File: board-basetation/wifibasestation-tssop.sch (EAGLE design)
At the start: 22 parts, among them IC1 1117EMP, J1 SWD_SHROUD_SMD, X1 ESP-03, X2 SMA-142-0711-821/826

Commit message: something changed
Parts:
- removed R1: 10k, passives-7351:RESISTOR0603-N
- removed R6: 4k7, passives-7351:RESISTOR0603-N
- added JP1: FTDI_BASICPTH, SparkFun-Connectors:FTDI_BASICPTH
- added RN2: 10k, resistor-dil:4R-NEXB38V
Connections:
- removed net N$18: R1.P$2, S1.1, U$1.BOOT0
- new net N$2: RN2B.1, S1.1, U$1.BOOT0
- new net N$8: RN2D.1, X1.GPIO2
- net +3V3: now also RN2D.2; no longer R6.P$1
- net GND: now also RN2A.2, RN2B.2, RN2C.2; no longer R1.P$1
- net GPIO0: now also RN2A.1
- net GPIO15: now also RN2C.1
- net N$1: no longer R6.P$2, X1.GPIO2
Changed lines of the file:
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@@
 <part name="C6" library="passives-7351" deviceset="CAPACITOR" device="0603-N" value="100n"/>
 <part name="C4" library="passives-7351" deviceset="CAPACITOR" device="0603-N" value="100n"/>
-<part name="R1" library="passives-7351" deviceset="RESISTOR" device="0603-N" value="10k"/>
 <part name="GND7" library="supply1" deviceset="GND" device=""/>
 <part name="J1" library="dtb" deviceset="SWD_SHROUD" device="_SMD" value="SWD_SHROUD_SMD"/>
@@
 <part name="GND22" library="supply1" deviceset="GND" device=""/>
 <part name="+3V14" library="supply1" deviceset="+3V3" device=""/>
-<part name="R6" library="passives-7351" deviceset="RESISTOR" device="0603-N" value="4k7"/>
 <part name="+3V15" library="supply1" deviceset="+3V3" device=""/>
 <part name="U$3" library="Mine" deviceset="ESP-07" device=""/>
@@
 <part name="+3V16" library="supply1" deviceset="+3V3" device=""/>
 <part name="U$1" library="dtb" deviceset="STM32F030F4" device=""/>
+<part name="RN2" library="resistor-dil" deviceset="4R-N" device="EXB38V" value="10k"/>
+<part name="GND1" library="supply1" deviceset="GND" device=""/>
+<part name="GND3" library="supply1" deviceset="GND" device=""/>
+<part name="JP1" library="SparkFun-Connectors" deviceset="FTDI_BASIC" device="PTH"/>
 </parts>
 <sheets>
@@
 <instance part="C6" gate="G$1" x="48.26" y="-25.4"/>
 <instance part="C4" gate="G$1" x="40.64" y="-25.4"/>
-<instance part="R1" gate="G$1" x="45.72" y="0" rot="R90"/>
-<instance part="GND7" gate="1" x="45.72" y="-7.62"/>
+<instance part="GND7" gate="1" x="45.72" y="-12.7"/>
 <instance part="J1" gate="G$1" x="30.48" y="142.24"/>
 <instance part="GND8" gate="1" x="12.7" y="132.08"/>
@@
 <instance part="GND22" gate="1" x="101.6" y="185.42"/>
 <instance part="+3V14" gate="G$1" x="101.6" y="236.22"/>
-<instance part="R6" gate="G$1" x="76.2" y="210.82"/>
-<instance part="+3V15" gate="G$1" x="68.58" y="210.82" rot="R90"/>
+<instance part="+3V15" gate="G$1" x="66.04" y="210.82" rot="R90"/>
 <instance part="U$3" gate="G$1" x="30.48" y="210.82"/>
 <instance part="GND23" gate="1" x="30.48" y="185.42"/>
 <instance part="+3V16" gate="G$1" x="30.48" y="236.22"/>
 <instance part="U$1" gate="G$1" x="76.2" y="-10.16"/>
+<instance part="RN2" gate="A" x="152.4" y="-12.7" rot="R270"/>
+<instance part="RN2" gate="C" x="78.74" y="190.5" rot="R270"/>
+<instance part="RN2" gate="D" x="76.2" y="210.82" rot="R180"/>
+<instance part="RN2" gate="B" x="45.72" y="-2.54" rot="R270"/>
+<instance part="GND1" gate="1" x="152.4" y="-22.86"/>
+<instance part="GND3" gate="1" x="78.74" y="180.34"/>
+<instance part="JP1" gate="G$1" x="177.8" y="2.54" rot="R180"/>
 </instances>
 <busses>
@@
 </segment>
 <segment>
-<pinref part="R1" gate="G$1" pin="P$1"/>
-<pinref part="GND7" gate="1" pin="GND"/>
-</segment>
-<segment>
 <pinref part="J1" gate="G$1" pin="GND1"/>
 <pinref part="GND8" gate="1" pin="GND"/>
@@
 <pinref part="U$3" gate="G$1" pin="GND"/>
 <pinref part="GND23" gate="1" pin="GND"/>
+</segment>
+<segment>
+<pinref part="RN2" gate="B" pin="2"/>
+<pinref part="GND7" gate="1" pin="GND"/>
+<wire x1="45.72" y1="-7.62" x2="45.72" y2="-10.16" width="0.1524" layer="91"/>
+</segment>
+<segment>
+<pinref part="RN2" gate="A" pin="2"/>
+<pinref part="GND1" gate="1" pin="GND"/>
+<wire x1="152.4" y1="-17.78" x2="152.4" y2="-20.32" width="0.1524" layer="91"/>
+</segment>
+<segment>
+<pinref part="RN2" gate="C" pin="2"/>
+<pinref part="GND3" gate="1" pin="GND"/>
+<wire x1="78.74" y1="185.42" x2="78.74" y2="182.88" width="0.1524" layer="91"/>
 </segment>
 </net>
@@
 </segment>
 <segment>
-<pinref part="R6" gate="G$1" pin="P$1"/>
-<pinref part="+3V15" gate="G$1" pin="+3V3"/>
-</segment>
-<segment>
 <pinref part="U$3" gate="G$1" pin="VCC"/>
 <pinref part="+3V16" gate="G$1" pin="+3V3"/>
+</segment>
+<segment>
+<pinref part="RN2" gate="D" pin="2"/>
+<pinref part="+3V15" gate="G$1" pin="+3V3"/>
+<wire x1="71.12" y1="210.82" x2="68.58" y2="210.82" width="0.1524" layer="91"/>
 </segment>
 </net>
@@
 <segment>
 <pinref part="X1" gate="G$1" pin="GPIO15"/>
-<wire x1="83.82" y1="200.66" x2="71.12" y2="200.66" width="0.1524" layer="91"/>
 <label x="71.12" y="200.66" size="1.778" layer="95"/>
+<wire x1="83.82" y1="200.66" x2="78.74" y2="200.66" width="0.1524" layer="91"/>
+<pinref part="RN2" gate="C" pin="1"/>
+<wire x1="78.74" y1="200.66" x2="71.12" y2="200.66" width="0.1524" layer="91"/>
+<wire x1="78.74" y1="195.58" x2="78.74" y2="200.66" width="0.1524" layer="91"/>
 </segment>
 <segment>
@@
 <segment>
 <label x="132.08" y="-2.54" size="1.778" layer="95"/>
-<wire x1="121.92" y1="-2.54" x2="134.62" y2="-2.54" width="0.1524" layer="91"/>
 <pinref part="U$1" gate="G$1" pin="PA4"/>
+<wire x1="121.92" y1="-2.54" x2="152.4" y2="-2.54" width="0.1524" layer="91"/>
+<pinref part="RN2" gate="A" pin="1"/>
+<wire x1="152.4" y1="-2.54" x2="154.94" y2="-2.54" width="0.1524" layer="91"/>
+<wire x1="152.4" y1="-7.62" x2="152.4" y2="-2.54" width="0.1524" layer="91"/>
 </segment>
 <segment>
@@
 <net name="N$1" class="0">
 <segment>
-<pinref part="X1" gate="G$1" pin="GPIO2"/>
-<pinref part="R6" gate="G$1" pin="P$2"/>
-<wire x1="83.82" y1="210.82" x2="81.28" y2="210.82" width="0.1524" layer="91"/>
-</segment>
-<segment>
 <wire x1="12.7" y1="210.82" x2="10.16" y2="210.82" width="0.1524" layer="91"/>
 <pinref part="U$3" gate="G$1" pin="GPIO2"/>
@@
 </segment>
 </net>
-<net name="N$18" class="0">
-<segment>
-<pinref part="R1" gate="G$1" pin="P$2"/>
+<net name="N$2" class="0">
+<segment>
+<pinref part="RN2" gate="B" pin="1"/>
 <pinref part="S1" gate="G$1" pin="1"/>
+<wire x1="45.72" y1="2.54" x2="45.72" y2="5.08" width="0.1524" layer="91"/>
 <pinref part="U$1" gate="G$1" pin="BOOT0"/>
 <wire x1="63.5" y1="-2.54" x2="50.8" y2="-2.54" width="0.1524" layer="91"/>
 <wire x1="50.8" y1="-2.54" x2="50.8" y2="5.08" width="0.1524" layer="91"/>
-<wire x1="50.8" y1="5.08" x2="45.72" y2="5.08" width="0.1524" layer="91"/>
-<junction x="45.72" y="5.08"/>
-</segment>
-</net>
+<wire x1="45.72" y1="5.08" x2="50.8" y2="5.08" width="0.1524" layer="91"/>
+</segment>
+</net>
+<net name="N$8" class="0">
+<segment>
+<pinref part="RN2" gate="D" pin="1"/>
+<pinref part="X1" gate="G$1" pin="GPIO2"/>
+<wire x1="81.28" y1="210.82" x2="83.82" y2="210.82" width="0.1524" layer="91"/>
+</segment>
+</net>

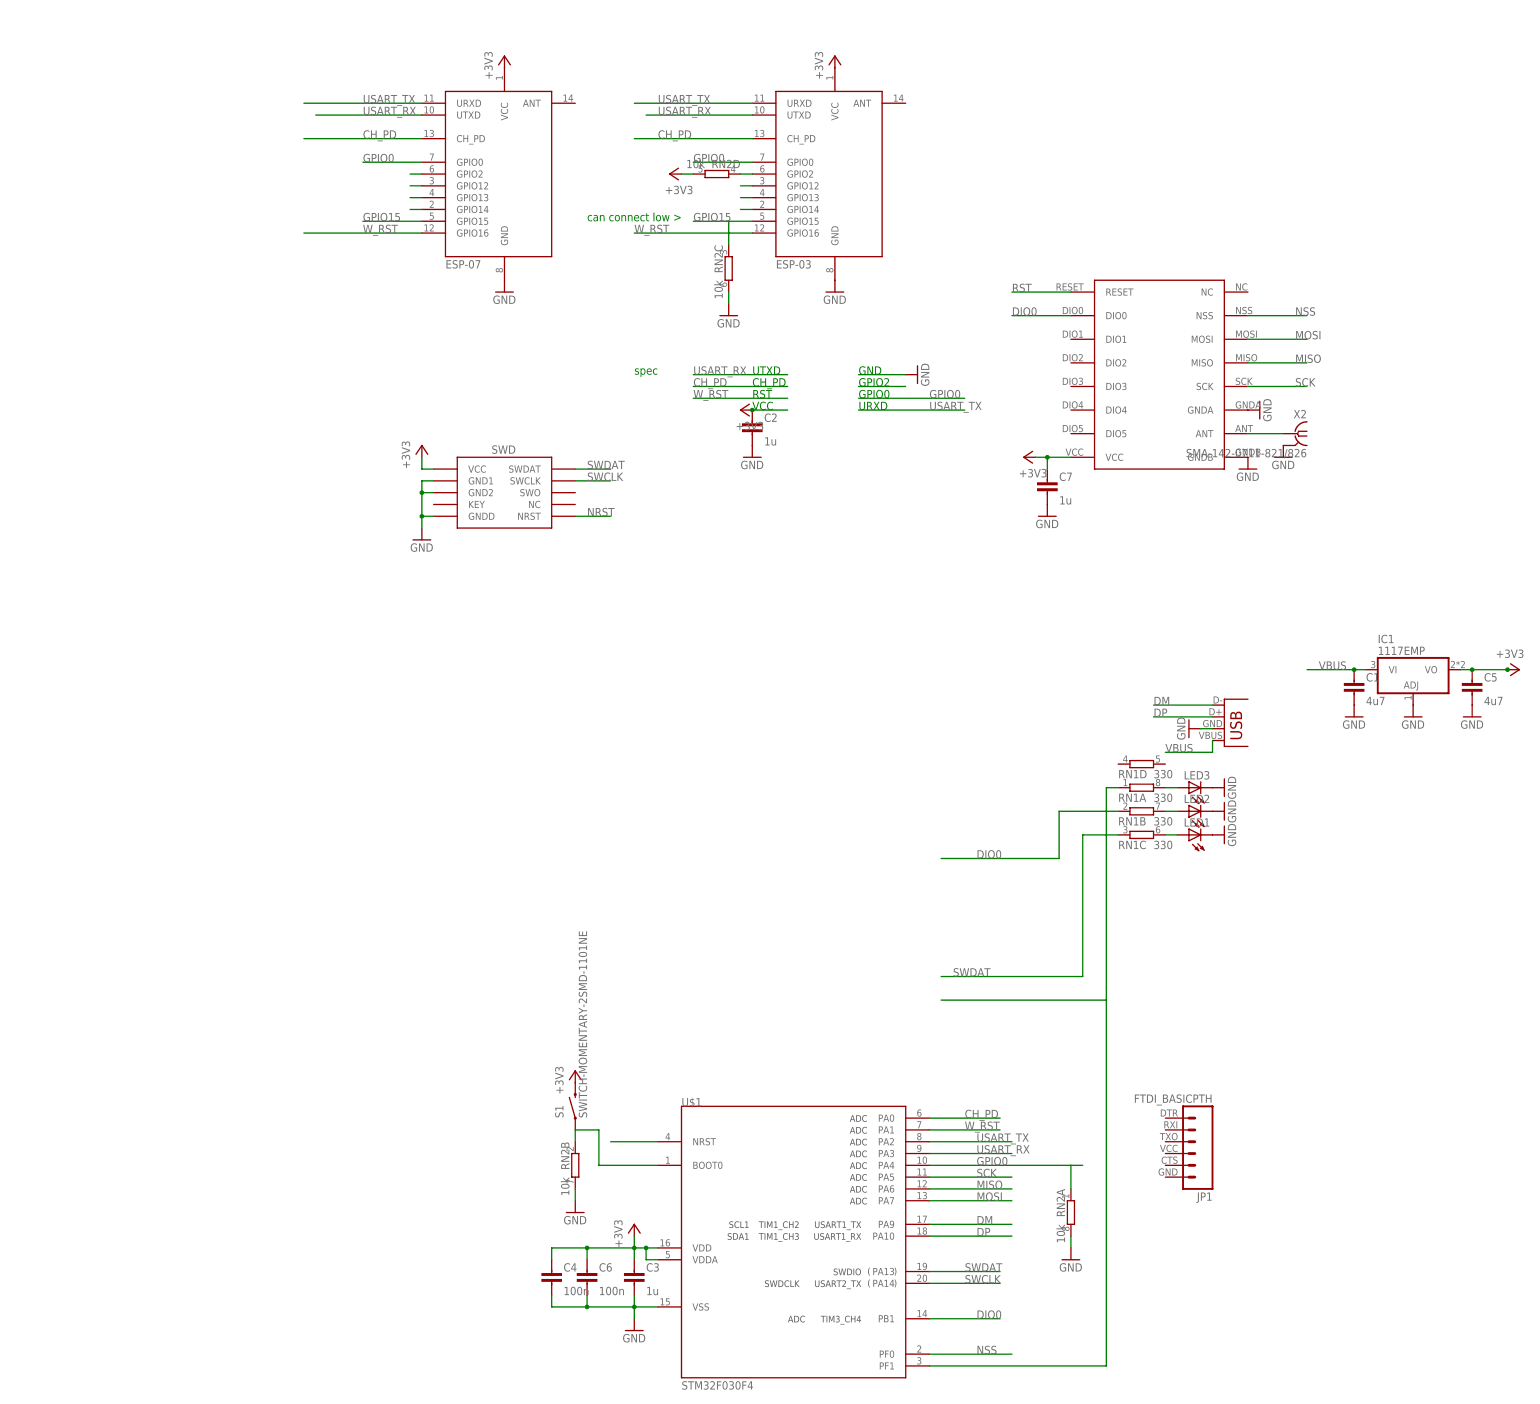
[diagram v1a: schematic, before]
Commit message: pretty much done tssop version
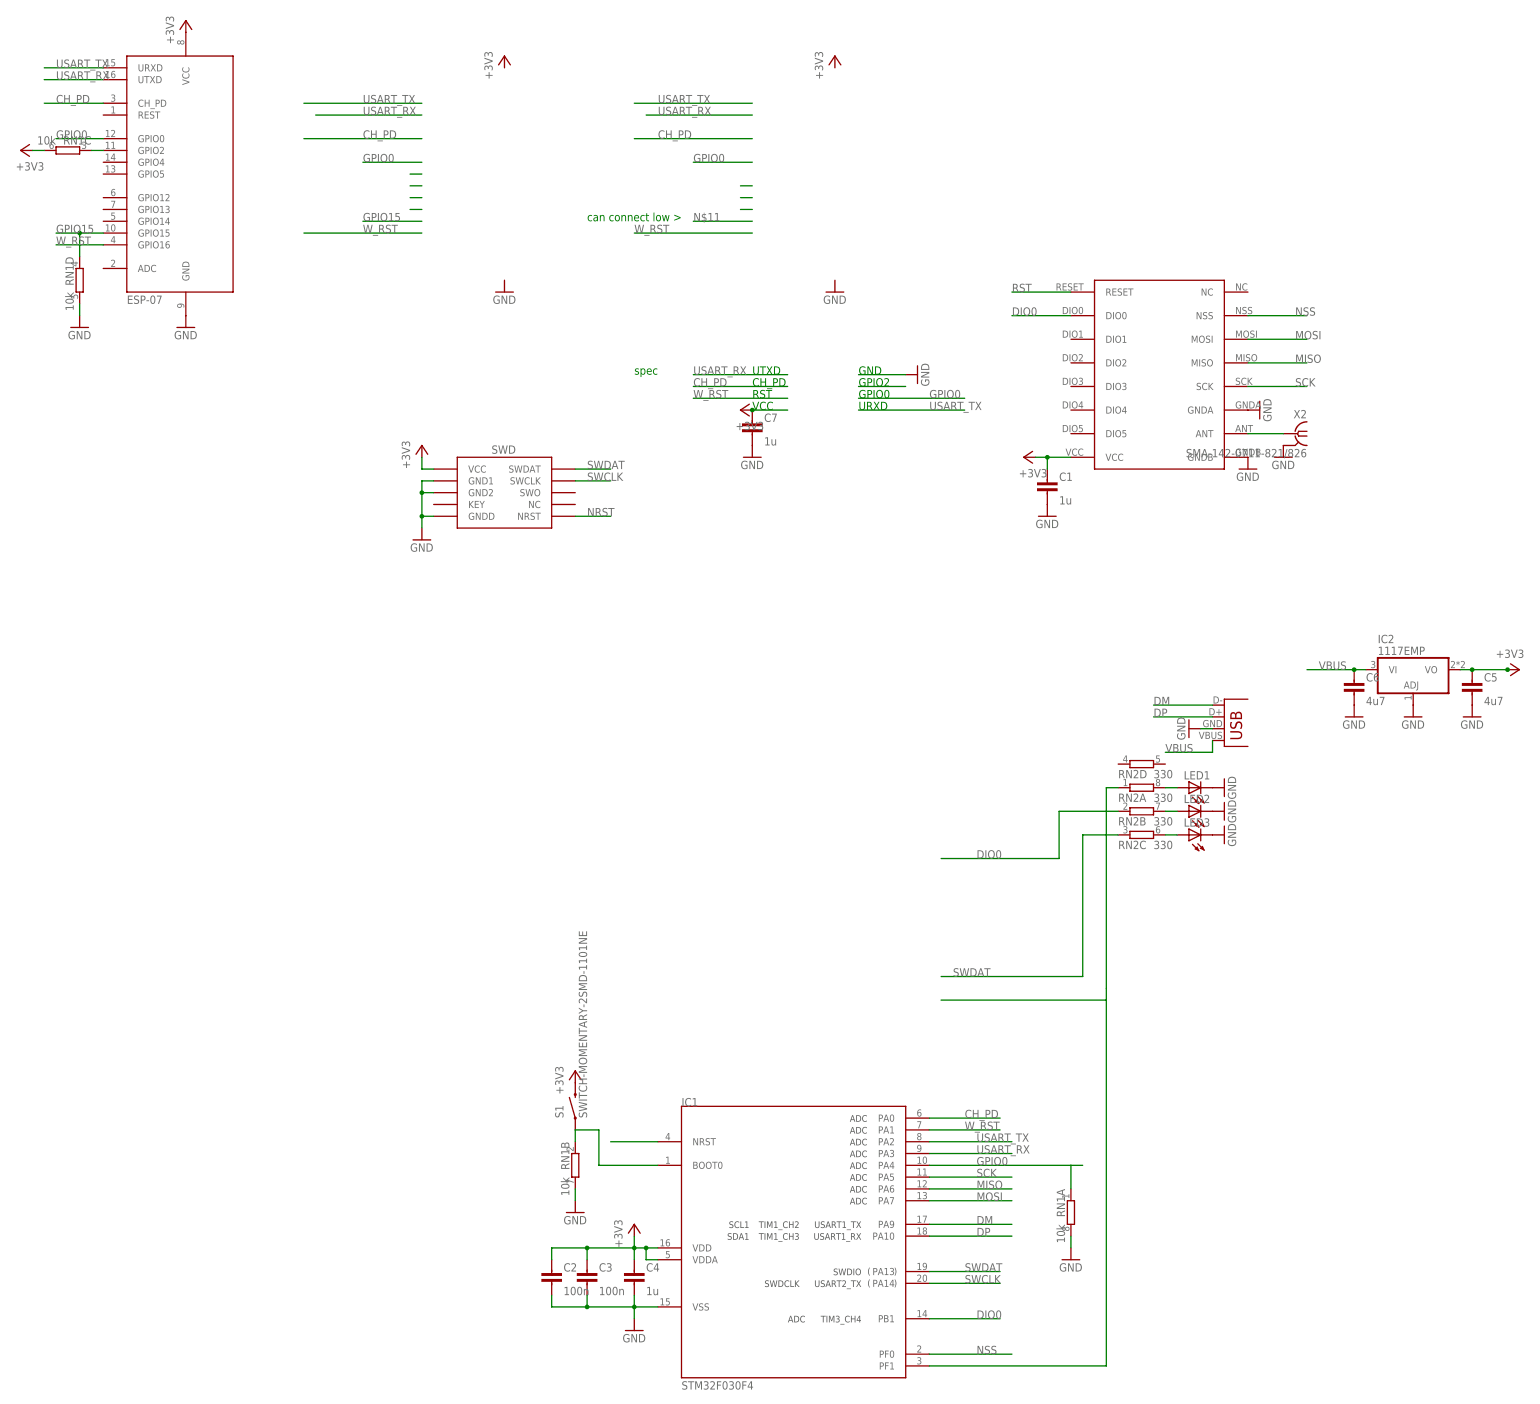
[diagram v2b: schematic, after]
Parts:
- removed JP3: USB-A-H, SparkFun-Connectors:USB-A-H
- removed U$2: RFM69HW, hoperf:RFM69HW
- removed U$3: ESP-07, Mine:ESP-07
- added IC2: 1117EMP, dtb:1117EMP
- C1: value 4u7 -> 1u
- C2, C3: value 1u -> 100n
- C4: value 100n -> 1u
- C6: value 100n -> 4u7
- IC1: value 1117EMP -> STM32F030F4; device dtb:1117EMP -> dtb:STM32F030F4
- JP1: value FTDI_BASICPTH -> USB-A-H; device SparkFun-Connectors:FTDI_BASICPTH -> SparkFun-Connectors:USB-A-H
- RN1: value 330 -> 10k
- RN2: value 10k -> 330
- U$1: value STM32F030F4 -> RFM69HW; device dtb:STM32F030F4 -> hoperf:RFM69HW
- X1: value ESP-03 -> ESP-07; device Mine:ESP-03 -> TiLDA Mk3 Parts:ESP-07
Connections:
- removed net N$1: U$3.GPIO2
- removed net N$3: U$3.GPIO14, X1.GPIO14
- removed net N$4: U$3.GPIO13, X1.GPIO13
- removed net N$7: U$3.GPIO12, X1.GPIO12
- net +3V3: now also C1.1, IC1.VDD, IC1.VDDA, IC2.VO, RN1C.2, U$1.VCC; no longer C6.1, IC1.VO, RN2D.2, U$1.VDD, U$1.VDDA, U$2.VCC, U$3.VCC
- net CH_PD: now also IC1.PA0; no longer U$1.PA0, U$3.CH_PD
- net DIO0: now also IC1.PB1, RN2B.1, U$1.DIO0; no longer RN1B.1, U$1.PB1, U$2.DIO0
- net DM: now also IC1.PA9, JP1.D+; no longer JP3.D+, U$1.PA9
- net DP: now also IC1.PA10, JP1.D-; no longer JP3.D-, U$1.PA10
- net GND: now also IC1.VSS, IC2.ADJ, JP1.VBUS, RN1A.2, RN1B.2, RN1D.2, U$1.GNDA, U$1.GNDB; no longer IC1.ADJ, JP3.VBUS, RN2A.2, RN2B.2, RN2C.2, U$1.VSS, U$2.GNDA, U$2.GNDB, U$3.GND
- net GPIO0: now also IC1.PA4, RN1A.1; no longer RN2A.1, U$1.PA4, U$3.GPIO0
- net GPIO15: now also RN1D.1; no longer RN2C.1, U$3.GPIO15
- net MISO: now also IC1.PA6, U$1.MISO; no longer U$1.PA6, U$2.MISO
- net MOSI: now also IC1.PA7, U$1.MOSI; no longer U$1.PA7, U$2.MOSI
- net N$10: now also RN2B.2; no longer RN1B.2
- net N$2: now also IC1.BOOT0, RN1B.1; no longer RN2B.1, U$1.BOOT0
- net N$20: now also LED3.A, RN2C.2; no longer LED1.A, RN1C.2
- net N$22: now also IC1.PF1, RN2A.1; no longer RN1A.1, U$1.PF1
- net N$6: now also U$1.ANT; no longer U$2.ANT
- net N$8: now also RN1C.1; no longer RN2D.1
- net N$9: now also LED1.A, RN2A.2; no longer LED3.A, RN1A.2
- net NRST: now also IC1.NRST; no longer U$1.NRST
- net NSS: now also IC1.PF0, U$1.NSS; no longer U$1.PF0, U$2.NSS
- net RST: now also U$1.RESET; no longer U$2.RESET
- net SCK: now also IC1.PA5, U$1.SCK; no longer U$1.PA5, U$2.SCK
- net SWCLK: now also IC1.PA14; no longer U$1.PA14
- net SWDAT: now also IC1.PA13, RN2C.1; no longer RN1C.1, U$1.PA13
- net USART_RX: now also IC1.PA3; no longer U$1.PA3, U$3.UTXD
- net USART_TX: now also IC1.PA2; no longer U$1.PA2, U$3.URXD
- net VBUS: now also C6.1, IC2.VI, JP1.GND; no longer C1.1, IC1.VI, JP3.GND
- net W_RST: now also IC1.PA1; no longer U$1.PA1, U$3.GPIO16
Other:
- moved on the sheet: C1, C2, C3, C4, C6, C7, LED1, LED3, RN1A, RN1B, RN1C, RN1D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
